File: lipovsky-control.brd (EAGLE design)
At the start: 59 x 32 mm, 47 parts, among them J5 AVRISP0.1", P1 M04-929P, P2 M04-929P, P3 M04-929P, P4 M04-929P, U1 ATTINYX4A8MU, U2 MIC2288YD5, U3 MIC2288YD5, U4 LTV-816S

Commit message: Label fix
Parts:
- renumbered U$2 to J1
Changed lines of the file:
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@@
 <attribute name="DIGIKEY_PART_#" value="541-4.70KLCT-ND" x="30.9" y="22.1" size="1.778" layer="27" rot="R180" display="off"/>
 </element>
-<element name="U$2" library="dubec" package="JUMPER-PAD-ROUND" value="JUMPER-PAD" x="33.4" y="21.2" rot="MR0"/>
+<element name="J1" library="dubec" package="JUMPER-PAD-ROUND" value="JUMPER-PAD" x="33.4" y="21.2" rot="MR0"/>
 </elements>
 <signals>
@@
 <wire x1="20.725" y1="18.925" x2="20.725" y2="16.995" width="0.25" layer="1"/>
 <wire x1="20.725" y1="16.995" x2="19.46" y2="15.73" width="0.25" layer="1"/>
-<contactref element="U$2" pad="2"/>
+<contactref element="J1" pad="2"/>
 <wire x1="33.1" y1="21.2" x2="29.4" y2="21.2" width="0.3" layer="16"/>
 <wire x1="29.4" y1="21.2" x2="26.5" y2="18.3" width="0.3" layer="16"/>
@@
 <signal name="!S_RESET">
 <contactref element="P3" pad="1"/>
-<contactref element="U$2" pad="1"/>
+<contactref element="J1" pad="1"/>
 <wire x1="42.2" y1="27.3" x2="36.1" y2="21.2" width="0.3" layer="16"/>
 <wire x1="36.1" y1="21.2" x2="33.7" y2="21.2" width="0.3" layer="16"/>

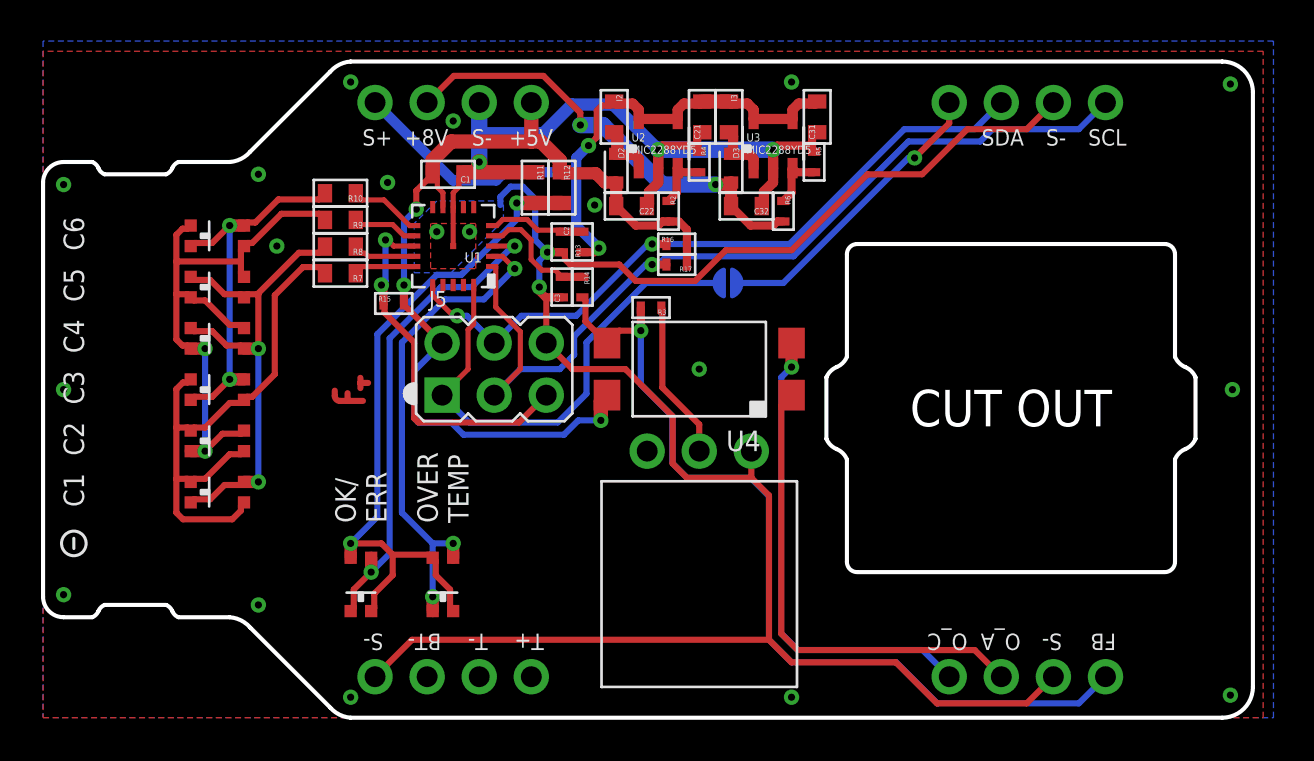
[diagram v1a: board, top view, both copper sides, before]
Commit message: Control board compacted
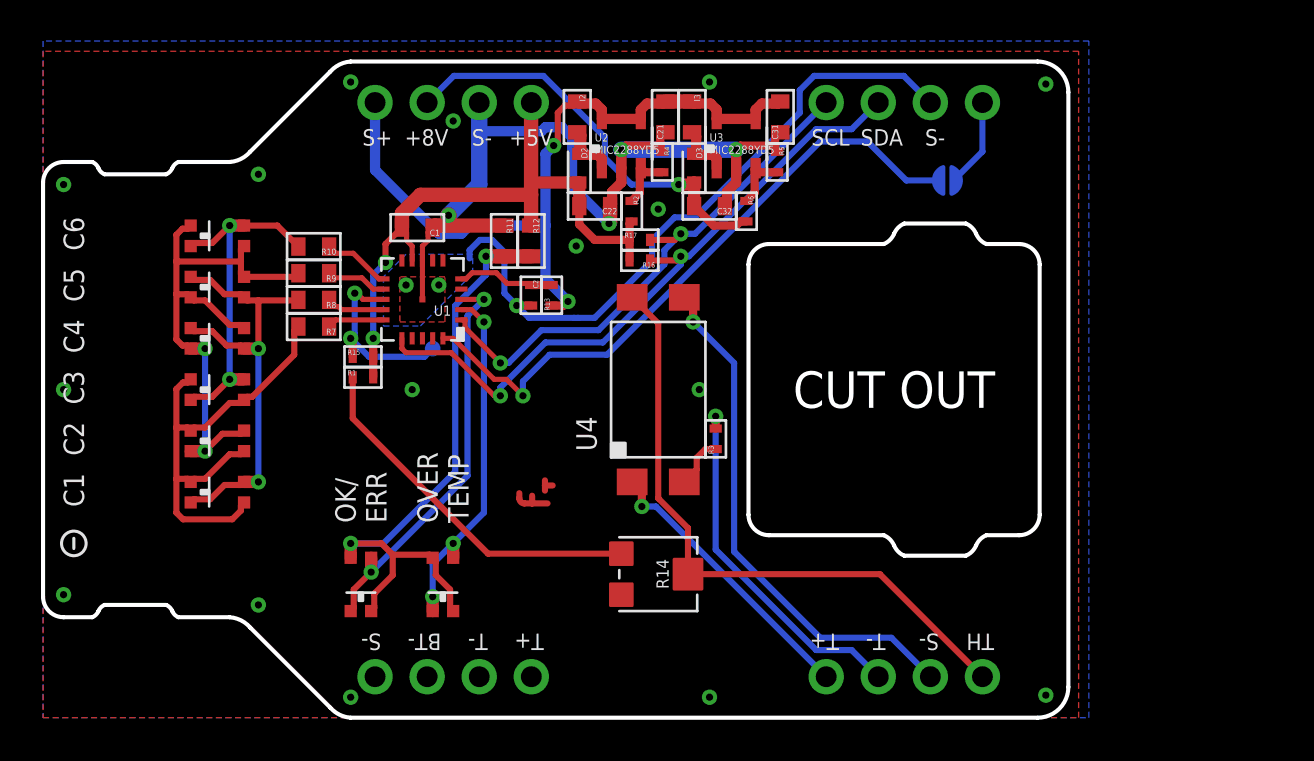
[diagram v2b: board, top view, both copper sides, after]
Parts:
- removed C3: CAP47N_50V, dubec:0402
- removed J5: AVRISP0.1", dubec:2X03
- added TP1: TEST-POINT3, SparkFun-Passives:PAD.03X.03
- R1: value POT5K -> RES7.5K_16; device dubec:3296W -> dubec:0402
- R14: value RES330_16 -> POT5K_TC33; device dubec:0402 -> dubec:TC33
- R3: value RES330_16 -> RES1.2K_16
- moved R1 16.8 mm to (15.6, 16.6)
- moved R14 14.5 mm to (30.0, 7.00)
- moved J1 11.8 mm to (44.1, 26.2)
- moved U$1 10.3 mm to (24.0, 11.0)
- moved R3 7.13 mm to (32.8, 13.6), turned to 90 degrees
- moved P2 6.00 mm to (42.0, 2.00)
- moved P3 6.00 mm to (42.0, 30.0)
- moved C1 3.00 mm to (18.2, 23.9)
- moved R11 3.00 mm to (22.5, 23.2)
- moved R12 3.00 mm to (23.8, 23.2)
- moved U1 3.00 mm to (18.5, 20.4)
- moved R15 3.00 mm to (15.6, 17.6)
- moved C2 3.00 mm to (23.8, 20.6)
- moved R13 3.00 mm to (24.8, 20.6)
- moved R7 2.91 mm to (13.2, 19.1)
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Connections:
- removed net FB: P2.1, R14.2, R3.2, U4.3
- removed net OPTO_A: P2.3, U4.1
- removed net OPTO_C: P2.4, U4.2
- new net N$8: R1.1, R14.CCW
- new net TH: P2.1, R14.WIPER, U4.4
- net !RESET: now also TP1.P$1; no longer J5.5
- net !S_RESET: now also P3.4; no longer P3.1
- net +5V: now also R1.2; no longer J5.2, U4.4
- net FB_ADC: no longer C3.2, R14.1
- net MISO: no longer J5.1
- net N$1: now also U4.2; no longer R1.WIPER
- net S-: now also U4.3; no longer C3.1, J5.6, P1.4, R1.CW
- net SCL: now also P3.1; no longer J5.3, P3.4
- net SDA: no longer J5.4
- net T+: now also P2.4, U4.1; no longer P1.1
- net T-: now also P2.3, R3.2; no longer P1.2
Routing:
- net FB: track 43.5 -> 0.00 mm, vias 1 -> 0
- net S-: track 138.8 -> 101.7 mm, vias 7 -> 8
- net TH: track 0.00 -> 31.1 mm
- net OPTO_C: track 23.4 -> 0.00 mm, vias 1 -> 0
- net OPTO_A: track 23.4 -> 0.00 mm
- net SCL: track 44.4 -> 26.2 mm, vias 1 -> 2
- net N$8: track 0.00 -> 17.8 mm
- net T-: track 0.00 -> 17.6 mm, vias 0 -> 1
- net +5V: track 46.7 -> 32.2 mm, vias 3 -> 2
- net T+: track 0.00 -> 13.8 mm, vias 0 -> 1
- net !S_RESET: track 14.7 -> 4.38 mm, vias 1 -> 0
- net !RESET: track 18.0 -> 9.29 mm
- net MISO: track 24.5 -> 31.8 mm, vias 0 -> 1
- net D_OVERTEMP: track 23.8 -> 17.2 mm
- net FB_ADC: track 6.03 -> 0.00 mm
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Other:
- board size 59 x 32 mm -> 50 x 32 mm
- board text added: "TH"
- board text removed: "FB"
- board text removed: "O_A"
- board text removed: "O_C"

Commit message: Control board fixes
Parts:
- R1: value RES7.5K_16 -> RES348_16
- R14: value POT5K_TC33 -> POT200
- R3: value RES1.2K_16 -> RES470_16
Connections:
- removed net FB_ADC: U1.4
- net D3: no longer D105.A2, D105.C1
- net D4: now also D105.A2, D105.C1
- net TH: now also U1.4
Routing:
- net TH: track 31.1 -> 41.4 mm
- net D4: track 16.6 -> 19.2 mm, vias 2 -> 4
- net D3: track 27.1 -> 26.0 mm
- net N$8: track 17.8 -> 17.3 mm

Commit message: tidy
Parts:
- renumbered I2 to L1, I3 to L2
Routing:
- net SCL: track 26.3 -> 25.2 mm
- net MISO: track 31.8 -> 30.7 mm
- net SDA: track 32.5 -> 31.5 mm

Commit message: Added choke
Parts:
- added U$2: CHOKE-102-2P, dubec:APC3225
- moved C2 1.00 mm to (24.8, 20.6)
- moved R13 1.00 mm to (23.8, 20.6)
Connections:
- new net S+F: C21.2, C31.2, L1.1, L2.1, U$2.P$4, U2.4, U2.5, U3.4, U3.5
- new net S-F: C1.1, C21.1, C22.1, C31.1, C32.1, R11.1, R4.1, R5.1, U$2.P$3, U1.8, U1.PAD, U2.2, U3.2
- net S+: now also U$2.P$1; no longer C21.2, C31.2, L1.1, L2.1, U2.4, U2.5, U3.4, U3.5
- net S-: now also U$2.P$2; no longer C1.1, C21.1, C22.1, C31.1, C32.1, R11.1, R4.1, R5.1, U1.8, U1.PAD, U2.2, U3.2
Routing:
- net S-F: track 0.00 -> 34.6 mm, vias 0 -> 6
- net S-: track 101.2 -> 66.7 mm, vias 8 -> 2
- net S+F: track 0.00 -> 19.3 mm, vias 0 -> 2
- net S+: track 37.5 -> 26.9 mm, vias 2 -> 1
- net +5V: track 32.3 -> 32.9 mm, vias 2 -> 3
- added copper zone on layer 1, net S-F
- added copper zone on layer 16, net S-F
- removed copper zone on layer 1, net S-
- removed copper zone on layer 16, net S-

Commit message: S-F
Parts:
- moved C2 9.79 mm to (16.7, 26.1), turned to 90 degrees
- moved R13 9.79 mm to (15.7, 26.1), turned to 270 degrees
- moved R6 0.64 mm to (34.7, 25.2)
- moved R2 0.64 mm to (29.1, 25.2)
- moved R16 0.64 mm to (29.5, 22.8)
- moved R17 0.64 mm to (29.5, 23.8)
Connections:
- net S-: no longer P2.2, P3.3, U4.3
- net S-F: now also P2.2, P3.3, U4.3
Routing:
- net S-: track 66.7 -> 7.69 mm, vias 2 -> 0
- net S-F: track 34.6 -> 82.2 mm, vias 6 -> 7
- net S+: track 26.9 -> 6.35 mm, vias 1 -> 0
- net S_ADC: track 4.77 -> 25.2 mm, vias 0 -> 2
- net TH: track 41.4 -> 39.8 mm
- net +8V: track 20.6 -> 21.6 mm
- net +5V: track 32.9 -> 33.8 mm
- net N$11: track 2.92 -> 2.25 mm
- net N$17: track 3.02 -> 2.37 mm

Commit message: routing
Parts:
- moved TP1 2.69 mm to (18.0, 15.5)
- moved C2 1.49 mm to (15.3, 25.6)
- moved R13 1.49 mm to (14.3, 25.6)
- moved U$2 1.49 mm to (18.6, 26.0)
- moved C1 0.20 mm to (18.2, 23.7)
- turned R1 to 180 degrees
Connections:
- removed net N$3: R10.1, U1.11
- removed net N$5: R8.1, U1.14
- removed net N$6: R7.1, U1.15
- removed net N$7: R9.1, U1.12
- new net D1L: D101.A1, D101.C2, D102.A1, D102.C2, D103.A1, D103.C2, R7.2
- new net D2L: D101.A2, D101.C1, D104.A1, D104.C2, D105.A1, D105.C2, R8.2
- new net D3L: D102.A2, D102.C1, D104.A2, D104.C1, D106.A1, D106.C2, R9.2
- new net D4L: D103.A2, D103.C1, D105.A2, D105.C1, D106.A2, D106.C1, R10.2
- net D1: now also R7.1, U1.15; no longer D101.A1, D101.C2, D102.A1, D102.C2, D103.A1, D103.C2, R7.2
- net D2: now also R8.1, U1.14; no longer D101.A2, D101.C1, D104.A1, D104.C2, D105.A1, D105.C2, R8.2
- net D3: now also R9.1, U1.12; no longer D102.A2, D102.C1, D104.A2, D104.C1, D106.A1, D106.C2, R9.2
- net D4: now also R10.1, U1.11; no longer D103.A2, D103.C1, D105.A2, D105.C1, D106.A2, D106.C1, R10.2
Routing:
- net D3L: track 0.00 -> 26.0 mm, vias 0 -> 2
- net D1L: track 0.00 -> 23.6 mm
- net D3: track 26.0 -> 2.97 mm, vias 2 -> 0
- net D2L: track 0.00 -> 22.0 mm, vias 0 -> 2
- net D1: track 23.6 -> 2.78 mm
- net D4L: track 0.00 -> 19.2 mm, vias 0 -> 4
- net D2: track 22.0 -> 2.85 mm, vias 2 -> 0
- net D4: track 19.2 -> 3.30 mm, vias 4 -> 0
- net N$3: track 3.30 -> 0.00 mm
- net N$7: track 2.97 -> 0.00 mm
- net N$5: track 2.85 -> 0.00 mm
- net N$6: track 2.78 -> 0.00 mm
- net TH: track 39.8 -> 42.5 mm
- net N$8: track 17.3 -> 19.5 mm
- net S-F: track 82.2 -> 84.1 mm, vias 7 -> 9
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
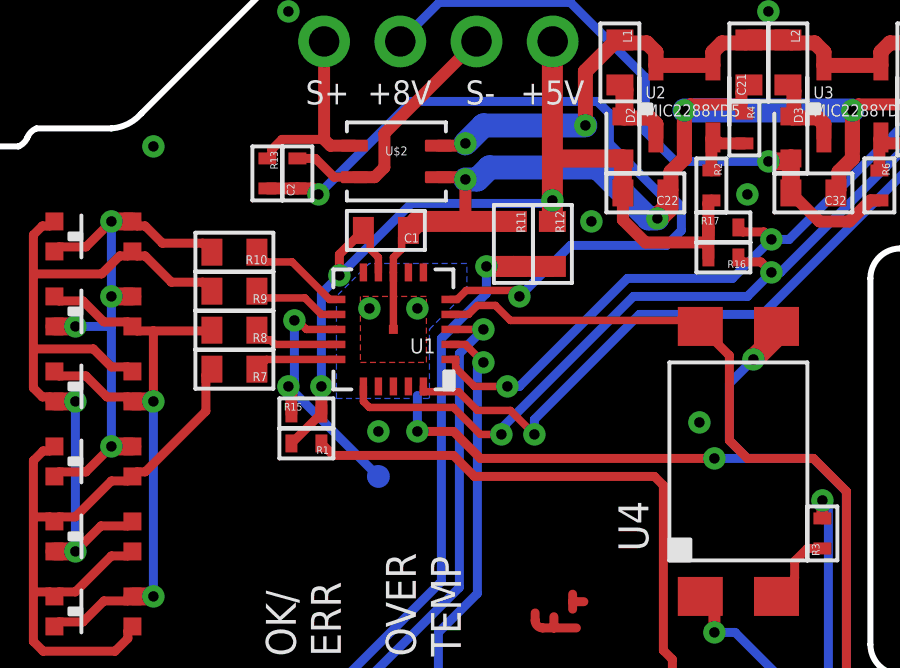
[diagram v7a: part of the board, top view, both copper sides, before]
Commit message: prog testpoints
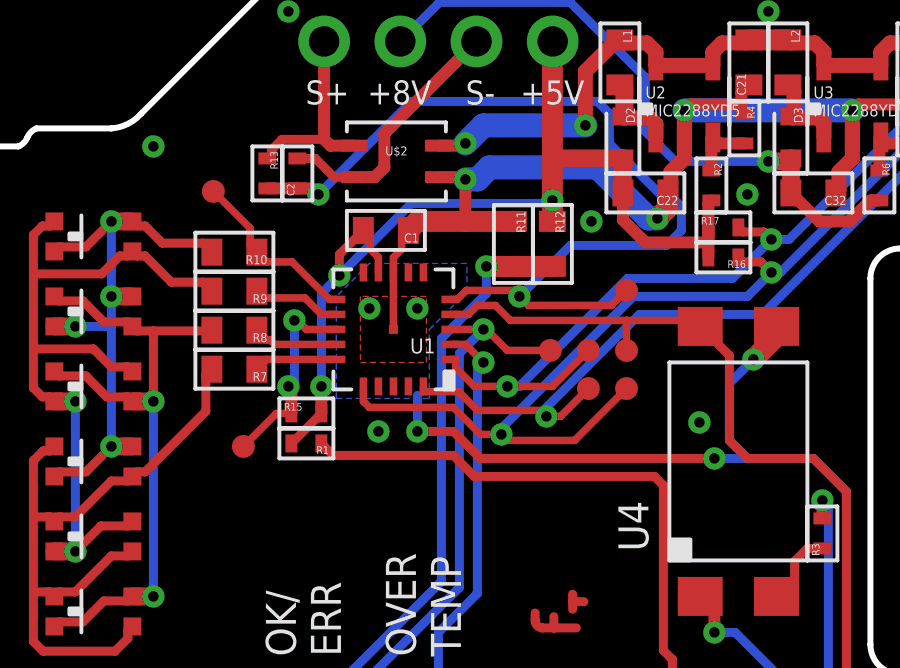
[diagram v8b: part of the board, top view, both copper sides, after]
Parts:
- removed TP1: TEST-POINT3, SparkFun-Passives:PAD.03X.03
- added TP_PA0, TP_PA1, TP_PA2, TP_PA4, TP_PA5, TP_PA6, TP_PB0, TP_PB3: TEST-POINT3, SparkFun-Passives:PAD.03X.03
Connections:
- net !RESET: now also TP_PB3.P$1; no longer TP1.P$1
- net D4: now also TP_PB0.P$1
- net D_STATUS: now also TP_PA2.P$1
- net MISO: now also TP_PA5.P$1
- net SCL: now also TP_PA4.P$1
- net SDA: now also TP_PA6.P$1
- net S_ADC: now also TP_PA0.P$1
- net TH: now also TP_PA1.P$1
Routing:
- net SDA: track 31.0 -> 36.0 mm
- net S_ADC: track 26.8 -> 30.7 mm
- net SCL: track 24.4 -> 27.6 mm
- net D4: track 3.30 -> 5.93 mm
- net D_STATUS: track 19.7 -> 22.2 mm
- net !RESET: track 8.99 -> 6.80 mm
- net MISO: track 30.8 -> 32.0 mm
- net TH: track 42.5 -> 43.5 mm
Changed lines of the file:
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@@
 </element>
 <element name="J1" library="dubec" package="JUMPER-PAD-ROUND" value="JUMPER-PAD" x="44.1" y="26.2" rot="MR0"/>
-<element name="TP1" library="SparkFun-Passives" package="PAD.03X.03" value="TEST-POINT3" x="18" y="15.5" rot="MR0"/>
+<element name="TP_PB3" library="SparkFun-Passives" package="PAD.03X.03" value="TEST-POINT3" x="13.5" y="16.5"/>
 <element name="R1" library="dubec" package="0402" value="RES348_16" x="15.6" y="16.6" rot="R180">
 <attribute name="MFG_PART_#" value="CRCW0402348RFKED" x="15.6" y="16.6" size="1.778" layer="27" rot="R180" display="off"/>
@@
 <attribute name="MANUFACTURER" value="TDK Corporation" x="18.6" y="26" size="1.778" layer="27" display="off"/>
 </element>
+<element name="TP_PA5" library="SparkFun-Passives" package="PAD.03X.03" value="TEST-POINT3" x="25" y="18.43"/>
+<element name="TP_PA0" library="SparkFun-Passives" package="PAD.03X.03" value="TEST-POINT3" x="26.27" y="21.7"/>
+<element name="TP_PA1" library="SparkFun-Passives" package="PAD.03X.03" value="TEST-POINT3" x="26.27" y="19.7"/>
+<element name="TP_PA2" library="SparkFun-Passives" package="PAD.03X.03" value="TEST-POINT3" x="23.73" y="19.7"/>
+<element name="TP_PB0" library="SparkFun-Passives" package="PAD.03X.03" value="TEST-POINT3" x="12.5" y="25"/>
+<element name="TP_PA4" library="SparkFun-Passives" package="PAD.03X.03" value="TEST-POINT3" x="25" y="19.7"/>
+<element name="TP_PA6" library="SparkFun-Passives" package="PAD.03X.03" value="TEST-POINT3" x="26.27" y="18.43"/>
 </elements>
 <signals>
@@
 <wire x1="15" y1="18.5" x2="15.1" y2="18.4" width="0.4" layer="1"/>
 <wire x1="15.1" y1="18.4" x2="15.1" y2="17.6" width="0.4" layer="1"/>
-<contactref element="TP1" pad="P$1"/>
-<wire x1="18" y1="15.5" x2="15" y2="18.5" width="0.3" layer="16"/>
+<contactref element="TP_PB3" pad="P$1"/>
+<wire x1="13.5" y1="16.5" x2="14.6" y2="17.6" width="0.25" layer="1"/>
+<wire x1="14.6" y1="17.6" x2="15.1" y2="17.6" width="0.25" layer="1"/>
 </signal>
 <signal name="+5V">
@@
 <contactref element="U1" pad="20"/>
 <contactref element="J1" pad="2"/>
-<via x="23.2" y="16.9" extent="1-16" drill="0.35"/>
+<via x="23.6" y="17.5" extent="1-16" drill="0.35"/>
 <wire x1="19.5" y1="18.5" x2="19.5" y2="18.325" width="0.25" layer="1"/>
 <wire x1="19.5" y1="18.325" x2="20.675" y2="18.325" width="0.25" layer="1"/>
 <wire x1="20.675" y1="18.325" x2="21.3" y2="17.7" width="0.25" layer="1"/>
-<wire x1="21.3" y1="17.7" x2="22.4" y2="17.7" width="0.25" layer="1"/>
-<wire x1="22.4" y1="17.7" x2="23.2" y2="16.9" width="0.25" layer="1"/>
-<wire x1="23.2" y1="16.9" x2="23.2" y2="17.4" width="0.3" layer="16"/>
-<wire x1="23.2" y1="17.4" x2="26.7" y2="20.9" width="0.3" layer="16"/>
+<wire x1="23.6" y1="17.5" x2="23.6" y2="17.8" width="0.3" layer="16"/>
+<wire x1="23.6" y1="17.8" x2="26.7" y2="20.9" width="0.3" layer="16"/>
 <wire x1="26.7" y1="20.9" x2="30.8" y2="20.9" width="0.3" layer="16"/>
 <wire x1="30.8" y1="20.9" x2="38" y2="28.1" width="0.3" layer="16"/>
 <wire x1="38" y1="28.1" x2="41.9" y2="28.1" width="0.3" layer="16"/>
 <wire x1="41.9" y1="28.1" x2="43.8" y2="26.2" width="0.3" layer="16"/>
+<wire x1="23.4" y1="17.7" x2="21.3" y2="17.7" width="0.25" layer="1"/>
+<contactref element="TP_PA5" pad="P$1"/>
+<wire x1="23.4" y1="17.7" x2="23.6" y2="17.5" width="0.25" layer="1"/>
+<wire x1="23.6" y1="17.5" x2="24.07" y2="17.5" width="0.25" layer="1"/>
+<wire x1="24.07" y1="17.5" x2="25" y2="18.43" width="0.25" layer="1"/>
 </signal>
 <signal name="S+">
@@
 <wire x1="20.7" y1="19.6" x2="20.7" y2="11.8" width="0.3" layer="16"/>
 <wire x1="20.7" y1="11.8" x2="16" y2="7.1" width="0.3" layer="16"/>
+<contactref element="TP_PA2" pad="P$1"/>
+<wire x1="21.5" y1="20.4" x2="21.6" y2="20.4" width="0.25" layer="1"/>
+<wire x1="21.6" y1="20.4" x2="22.3" y2="19.7" width="0.25" layer="1"/>
+<wire x1="22.3" y1="19.7" x2="23.73" y2="19.7" width="0.25" layer="1"/>
 </signal>
 <signal name="D_OVERTEMP">
@@
 <wire x1="27.6" y1="23.2" x2="24.4" y2="23.2" width="0.3" layer="16"/>
 <wire x1="24.4" y1="23.2" x2="22.7" y2="21.5" width="0.3" layer="16"/>
+<contactref element="TP_PA0" pad="P$1"/>
+<wire x1="22.7" y1="21.5" x2="23" y2="21.2" width="0.25" layer="1"/>
+<wire x1="23" y1="21.2" x2="25.77" y2="21.2" width="0.25" layer="1"/>
+<wire x1="25.77" y1="21.2" x2="26.27" y2="21.7" width="0.25" layer="1"/>
 </signal>
 <signal name="D4">
@@
 <contactref element="U1" pad="11"/>
 <wire x1="16.375" y1="21.4" x2="16.6" y2="21.4" width="0.25" layer="1"/>
+<contactref element="TP_PB0" pad="P$1"/>
+<wire x1="12.5" y1="25" x2="13.725" y2="23.775" width="0.25" layer="1"/>
+<wire x1="13.725" y1="23.775" x2="13.725" y2="23.2" width="0.25" layer="1"/>
+<wire x1="13.725" y1="23.2" x2="13.95" y2="22.975" width="0.25" layer="1"/>
 </signal>
 <signal name="D3">
@@
 <wire x1="30.15" y1="22.65" x2="30.75" y2="22.65" width="0.3" layer="1"/>
 <wire x1="30.75" y1="22.65" x2="31.1" y2="22.3" width="0.3" layer="1"/>
+<contactref element="TP_PA6" pad="P$1"/>
+<wire x1="24.54" y1="16.7" x2="22.3" y2="16.7" width="0.25" layer="1"/>
+<wire x1="22.3" y1="16.7" x2="22.1" y2="16.9" width="0.25" layer="1"/>
+<wire x1="24.54" y1="16.7" x2="26.27" y2="18.43" width="0.25" layer="1"/>
 </signal>
 <signal name="SCL">
@@
 <wire x1="30.85" y1="23.65" x2="31.1" y2="23.4" width="0.3" layer="1"/>
 <wire x1="29.8" y1="22.1" x2="31.1" y2="23.4" width="0.3" layer="16"/>
+<contactref element="TP_PA4" pad="P$1"/>
+<wire x1="23.8" y1="18.5" x2="22.3" y2="18.5" width="0.25" layer="1"/>
+<wire x1="23.8" y1="18.5" x2="25" y2="19.7" width="0.25" layer="1"/>
 </signal>
 <signal name="!S_RESET">
@@
 <wire x1="21.3" y1="21.2" x2="21.9" y2="21.2" width="0.25" layer="1"/>
 <wire x1="21.9" y1="21.2" x2="22.4" y2="20.7" width="0.25" layer="1"/>
-<wire x1="22.4" y1="20.7" x2="28.53" y2="20.7" width="0.25" layer="1"/>
+<wire x1="22.4" y1="20.7" x2="26.27" y2="20.7" width="0.25" layer="1"/>
+<wire x1="26.27" y1="20.7" x2="28.53" y2="20.7" width="0.25" layer="1"/>
 <wire x1="28.53" y1="20.7" x2="28.73" y2="20.5" width="0.25" layer="1"/>
 <wire x1="45.81" y1="2" x2="43.91" y2="3.9" width="0.3" layer="1"/>
@@
 <wire x1="29.7" y1="16.7" x2="30.3" y2="16.1" width="0.3" layer="1"/>
 <wire x1="30.3" y1="16.1" x2="32.5" y2="16.1" width="0.3" layer="1"/>
+<contactref element="TP_PA1" pad="P$1"/>
+<wire x1="26.27" y1="19.7" x2="26.27" y2="20.7" width="0.25" layer="1"/>
 </signal>
 <signal name="N$1">
